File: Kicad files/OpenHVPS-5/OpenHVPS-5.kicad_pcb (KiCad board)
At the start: 2 copper layers, 40.6 x 20.8 mm, 82 parts, among them J1 Conn_01x03_Male, Q1 FQT7N10, Q2 BC846A, Q3 MMDT3906, U1 MAX6008AEUR+T, U2 74HC14, U3 MAX4162, U4 CD14538BM

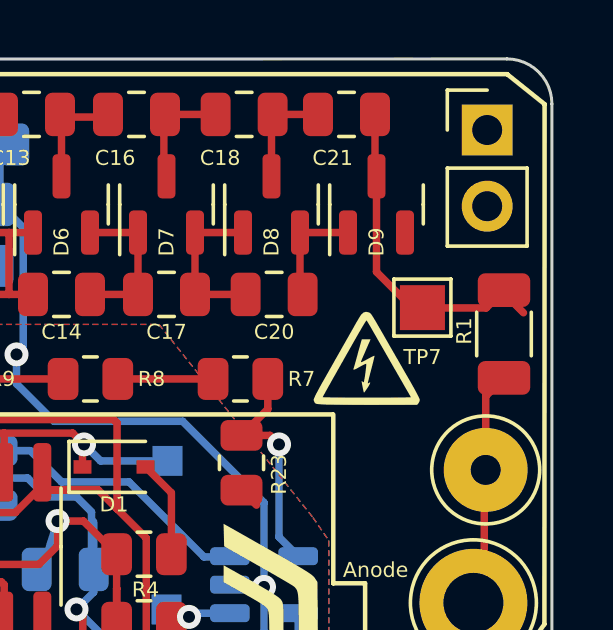
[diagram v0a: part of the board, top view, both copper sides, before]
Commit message: Moved TP7 to other side of board.
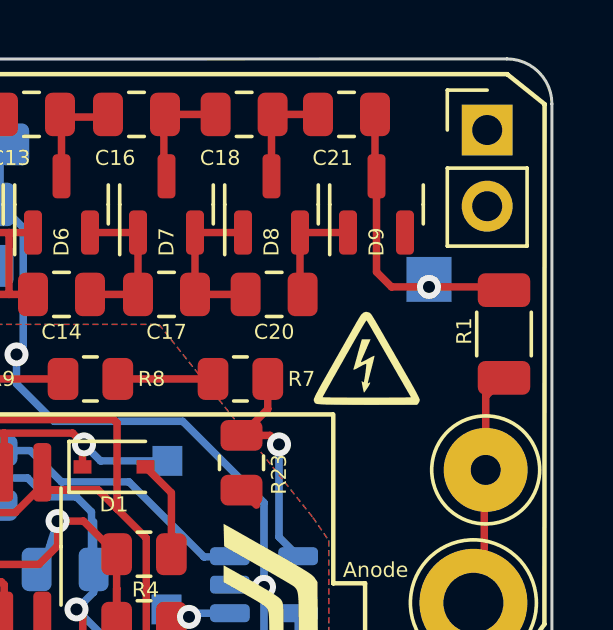
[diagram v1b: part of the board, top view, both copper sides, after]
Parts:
- TP7: moved to B.Cu
- moved TP7 0.97 mm to (162.8, 64.5), turned to 180 degrees
- moved G*** 0.61 mm to (164.5, 66.8)
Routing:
- net Net-(C21-Pad2): track 10.7 -> 10.5 mm, vias 0 -> 1
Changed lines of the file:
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@@
     )
   )
-  (footprint "TestPoint:TestPoint_Pad_1.5x1.5mm" (layer "F.Cu")
-    (at 162.53 65.44)
-    (descr "SMD rectangular pad as test Point, square 1.5mm side length")
-    (tags "test point SMD pad rectangle square")
-    (property "Sheet file" "OpenHVPS-5.kicad_sch")
-    (property "Sheet name" "")
-    (property "exclude_from_bom" "")
-    (attr exclude_from_pos_files exclude_from_bom)
-    (fp_text reference "TP7" (at 0 1.65 180) (layer "F.SilkS")
-      (effects (font (size 0.5 0.5) (thickness 0.075)))
-    )
-    (fp_text value "TestPoint" (at 0 1.75) (layer "F.Fab") hide
-      (effects (font (size 1 1) (thickness 0.15)))
-    )
-    (fp_text user "${REFERENCE}" (at 0 -1.65) (layer "F.Fab")
-      (effects (font (size 1 1) (thickness 0.15)))
-    )
-    (fp_line (start -0.95 0.95) (end -0.95 -0.95) (layer "F.SilkS") (width 0.12))
-    (fp_line (start 0.95 0.95) (end -0.95 0.95) (layer "F.SilkS") (width 0.12))
-    (fp_line (start 0.95 -0.95) (end 0.95 0.95) (layer "F.SilkS") (width 0.12))
-    (fp_line (start -0.95 -0.95) (end 0.95 -0.95) (layer "F.SilkS") (width 0.12))
-    (fp_line (start 1.25 1.25) (end 1.25 -1.25) (layer "F.CrtYd") (width 0.05))
-    (fp_line (start 1.25 1.25) (end -1.25 1.25) (layer "F.CrtYd") (width 0.05))
-    (fp_line (start -1.25 -1.25) (end 1.25 -1.25) (layer "F.CrtYd") (width 0.05))
-    (fp_line (start -1.25 -1.25) (end -1.25 1.25) (layer "F.CrtYd") (width 0.05))
-    (pad "1" smd rect (at 0 0) (locked) (size 1.5 1.5) (layers "F.Cu" "F.Mask")
-      (net 25 "Net-(C21-Pad2)") (pinfunction "1"))
-  )
   (footprint "Capacitor_SMD:C_0805_2012Metric" (layer "F.Cu")
     (at 130.5 60 -90)
@@
   )
   (footprint "Symbol:HV warning" (layer "B.Cu")
-    (at 163.99 66.42 180)
+    (at 164.5 66.75 180)
     (attr through_hole)
     (fp_text reference "G***" (at 0 0) (layer "B.SilkS") hide
@@
       (net 27 "+2V5") (pinfunction "1"))
   )
+  (footprint "TestPoint:TestPoint_Pad_1.5x1.5mm" (layer "B.Cu")
+    (at 162.75 64.5 180)
+    (descr "SMD rectangular pad as test Point, square 1.5mm side length")
+    (tags "test point SMD pad rectangle square")
+    (property "Sheet file" "OpenHVPS-5.kicad_sch")
+    (property "Sheet name" "")
+    (property "exclude_from_bom" "")
+    (attr exclude_from_pos_files exclude_from_bom)
+    (fp_text reference "TP7" (at 0 1.75 180) (layer "B.SilkS")
+      (effects (font (size 0.5 0.5) (thickness 0.075)) (justify mirror))
+    )
+    (fp_text value "TestPoint" (at 0 -1.75) (layer "B.Fab") hide
+      (effects (font (size 1 1) (thickness 0.15)) (justify mirror))
+    )
+    (fp_text user "${REFERENCE}" (at 0 1.65) (layer "B.Fab") hide
+      (effects (font (size 1 1) (thickness 0.15)) (justify mirror))
+    )
+    (fp_line (start -0.95 -0.95) (end -0.95 0.95) (layer "B.SilkS") (width 0.12))
+    (fp_line (start 0.95 -0.95) (end -0.95 -0.95) (layer "B.SilkS") (width 0.12))
+    (fp_line (start 0.95 0.95) (end 0.95 -0.95) (layer "B.SilkS") (width 0.12))
+    (fp_line (start -0.95 0.95) (end 0.95 0.95) (layer "B.SilkS") (width 0.12))
+    (fp_line (start 1.25 -1.25) (end 1.25 1.25) (layer "B.CrtYd") (width 0.05))
+    (fp_line (start 1.25 -1.25) (end -1.25 -1.25) (layer "B.CrtYd") (width 0.05))
+    (fp_line (start -1.25 1.25) (end 1.25 1.25) (layer "B.CrtYd") (width 0.05))
+    (fp_line (start -1.25 1.25) (end -1.25 -1.25) (layer "B.CrtYd") (width 0.05))
+    (pad "1" smd rect (at 0 0 180) (locked) (size 1.5 1.5) (layers "B.Cu" "B.Mask")
+      (net 25 "Net-(C21-Pad2)") (pinfunction "1"))
+  )
   (footprint "Resistor_SMD:R_0805_2012Metric" (layer "B.Cu")
     (at 148.336 71.12 90)
@@
   (segment (start 143 66.75) (end 142.5 67.25) (width 0.25) (layer "B.Cu") (net 24))
   (segment (start 142.5 69.1855) (end 141.96775 69.71775) (width 0.25) (layer "B.Cu") (net 24))
+  (segment (start 161 64.25) (end 161.5 64.75) (width 0.25) (layer "F.Cu") (net 25))
+  (segment (start 164.8575 65.25) (end 165.25 64.8575) (width 0.25) (layer "F.Cu") (net 25))
   (segment (start 160.95 59) (end 160.95 61.0125) (width 0.25) (layer "F.Cu") (net 25))
+  (segment (start 161.5 64.75) (end 162.75 64.75) (width 0.25) (layer "F.Cu") (net 25))
   (segment (start 160.95 61.0125) (end 161 61.0625) (width 0.25) (layer "F.Cu") (net 25))
   (segment (start 160.912 59) (end 160.9123 59.0002) (width 0.25) (layer "F.Cu") (net 25))
-  (segment (start 165.9 65.6125) (end 165.6125 65.325) (width 0.25) (layer "F.Cu") (net 25))
-  (segment (start 162.075 65.325) (end 161 64.25) (width 0.25) (layer "F.Cu") (net 25))
-  (segment (start 162.775 65.45) (end 164.6575 65.45) (width 0.25) (layer "F.Cu") (net 25))
-  (segment (start 164.6575 65.45) (end 165.25 64.8575) (width 0.25) (layer "F.Cu") (net 25))
+  (segment (start 162.75 64.75) (end 165.1425 64.75) (width 0.25) (layer "F.Cu") (net 25))
+  (segment (start 165.1425 64.75) (end 165.25 64.8575) (width 0.25) (layer "F.Cu") (net 25))
   (segment (start 161 64.25) (end 161 61.0625) (width 0.25) (layer "F.Cu") (net 25))
   (segment (start 160.9123 59.0002) (end 161 59.0875) (width 0.25) (layer "F.Cu") (net 25))
-  (segment (start 162.6875 65.325) (end 162.075 65.325) (width 0.25) (layer "F.Cu") (net 25))
   (segment (start 160.9125 59) (end 160.9123 59.0002) (width 0.25) (layer "F.Cu") (net 25))
+  (via (at 162.75 64.75) (size 0.8) (drill 0.4) (layers "F.Cu" "B.Cu") (net 25))
   (segment (start 144.414 69.624) (end 143.51 70.5278) (width 0.25) (layer "F.Cu") (net 26))
   (segment (start 144.78 75.881) (end 143.51 75.881) (width 0.25) (layer "F.Cu") (net 26))
